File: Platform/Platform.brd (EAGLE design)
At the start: 97.8 x 36.8 mm, 30 parts, among them U1 LCD-16X2NOSILK, U2 LM2574N, X1 USBSMD, Y1 RESONATORSMD

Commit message: prototype 3
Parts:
- removed C10: 220uf, SparkFun:CPOL-RADIAL-100UF-25V
- removed C7: 4.7uf, SparkFun:CPOL-RADIAL-100UF-25V
- removed LOGO1: OSHW_LOGO_10MIL, ohw-logo:OSHW_10X200_NOTEXT_COPPER
- removed SG1: BUZZERPTH, SparkFun:BUZZER-12MM
- removed U1: LCD-16X2NOSILK, SparkFun:LCD-16X2_NOSILK
- added C4: 68uf, Dustin:F80
- added C5: 120uf, Dustin:10X8CAP
- added JP1: M14B, Dustin:1X14B
- added LCDCON: (no value), con-harting:CON14
- added LED2: RED, SparkFun:LED-1206
- added LINK1, LINK2, LINK3, LINK4: LINK, Dustin:ISOLATOR
- added R4: TRIMPOTSMD, SparkFun:TRIMPOT-3MM
- added SG2: BUZZERSMD, SparkFun:BUZZER-CMT1603
- C8: value 22uf -> 4.7uf; device SparkFun:CPOL-RADIAL-100UF-25V -> Dustin:CAP-B
- L2: value 330uH -> 100uH; device SparkFun:INDUCTOR-1206 -> SparkFun:0805
- LED1: value (none) -> GRN; device SparkFun:LED3MM -> SparkFun:LED-1206
- R3: value 10k -> 220; device SparkFun:TRIM_POT_PTH -> SparkFun:0805
- SCHOTTKEY: value 11DQ06 -> (none); device SparkFun:DIODE-ZENER -> Dustin:SOD-123
- U$1: value FT232RL -> FT232RLSSOP; device Dustin:TSSOP28 -> Dustin:SSOP28
- U$4: value DCJACK -> DCJACKSMD; device Dustin:DCPOWERSOCKETPJ-019 -> Dustin:JACK-SMD
- U2: device Dustin:8DILL -> Dustin:SOIC8
- moved S1 70.1 mm to (69.1, 41.3), turned to 0 degrees
- moved LED1 37.5 mm to (60.7, 41.7), turned to 0 degrees
- moved C2 33.8 mm to (33.4, 16.2)
- moved R1 32.8 mm to (31.2, 16.0)
- moved R3 31.0 mm to (61.2, 39.1)
- moved C8 24.4 mm to (60.5, 26.2), turned to 0 degrees
- moved SPI 20.6 mm to (14.0, 5.16), turned to 0 degrees
- moved U$4 12.9 mm to (25.4, -2.33), turned to 0 degrees
- moved C9 11.8 mm to (68.1, 26.7), turned to 0 degrees
- moved C1 11.4 mm to (64.7, 26.6)
- moved U$1 9.96 mm to (65.5, 18.0), turned to 0 degrees
- moved SCHOTTKEY 7.06 mm to (50.8, 2.54)
- moved U2 6.59 mm to (52.0, 7.11)
- moved L2 6.34 mm to (44.2, 12.6), turned to 0 degrees
- moved C6 6.28 mm to (73.4, 10.1), turned to 90 degrees
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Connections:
- removed net CTS: U$1.11
- new net FTDI-GND: C8.-, C9.1, LINK4.P$2, U$1.11, U$1.18, U$1.21, U$1.25, U$1.26, U$1.7
- new net FTDI-VCC: C6.-, C8.+, LINK3.P$1, U$1.20, U$1.4, U$3.2, X1.GND
- new net GNDLINK: C4.-, C5.-, LINK2.P$1, SCHOTTKEY.ANODE, U2.2, U2.3, U2.4
- new net N$7: LED1.C, R3.2
- new net VCCLINK: C5.+, L2.2, LINK1.P$1, U2.1
- net A1: now also JP1.3
- net A2: now also JP1.4
- net A3: now also JP1.5
- net A4: now also JP1.6
- net A5: now also JP1.7
- net A6: now also JP1.8
- net A7: now also JP1.9
- net CONTRAST: now also LCDCON.3, R4.2; no longer R3.2, U1.3
- net D10: now also LCDCON.4; no longer U1.4
- net D13/SCK: now also JP1.13, LED2.A; no longer LED1.A
- net D3: now also JP1.12
- net D4: now also LCDCON.14; no longer U1.14
- net D5: now also SG2.P$2; no longer SG1.-
- net D6: now also LCDCON.13; no longer U1.13
- net D7: now also LCDCON.12; no longer U1.12
- net D8: now also LCDCON.11; no longer U1.11
- net D9: now also LCDCON.6; no longer U1.6
- net GND: now also JP1.1, LCDCON.1, LCDCON.5, LINK2.P$2, LINK4.P$1, R3.1, R4.3, SG2.P$1; no longer C10.2, C6.-, C7.2, C8.2, C9.1, R3.3, SCHOTTKEY.P$2, SG1.+, U$1.18, U$1.21, U$1.25, U$1.26, U$1.7, U1.1, U1.16, U1.5, U2.2, U2.3, U2.4, X1.GND
- net N$2: now also LED2.C; no longer LED1.K
- net N$3: now also L2.1, SCHOTTKEY.CATHODE; no longer L2.P$1, SCHOTTKEY.P$1
- net RAW: now also C4.+; no longer C8.1
- net RAW_IN: now also U$4.1A, U$4.1B; no longer U$4.1C
- net RESET: now also JP1.14
- net RX: now also JP1.10
- net TX: now also JP1.11
- net VCC: now also JP1.2, LCDCON.2, LED1.A, LINK1.P$2, LINK3.P$2, R4.1; no longer C10.1, C7.1, L2.P$2, R3.1, U$1.20, U$1.4, U$3.2, U1.15, U1.2, U2.1
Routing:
- net FTDI-VCC: track 0.00 -> 65.2 mm
- net GNDLINK: track 0.00 -> 57.8 mm
- net RESET: track 86.6 -> 53.2 mm, vias 2 -> 0
- net D13/SCK: track 155.3 -> 122.1 mm, vias 1 -> 2
- net FTDI-GND: track 0.00 -> 33.2 mm
- net DTR: track 5.71 -> 32.8 mm
- net A0: track 108.1 -> 134.2 mm
- net VCC: track 236.7 -> 262.9 mm
- net VCCLINK: track 0.00 -> 25.6 mm
- net D11/MOSI: track 60.1 -> 35.5 mm
- net D12/MISO: track 99.6 -> 119.6 mm
- net RAW_IN: track 42.3 -> 62.0 mm, vias 0 -> 1
- net GND: track 331.7 -> 350.1 mm, vias 0 -> 2
- net N$4: track 34.4 -> 17.7 mm
- net N$5: track 33.8 -> 17.5 mm
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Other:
- board size 97.8 x 36.8 mm -> 91.7 x 42.9 mm

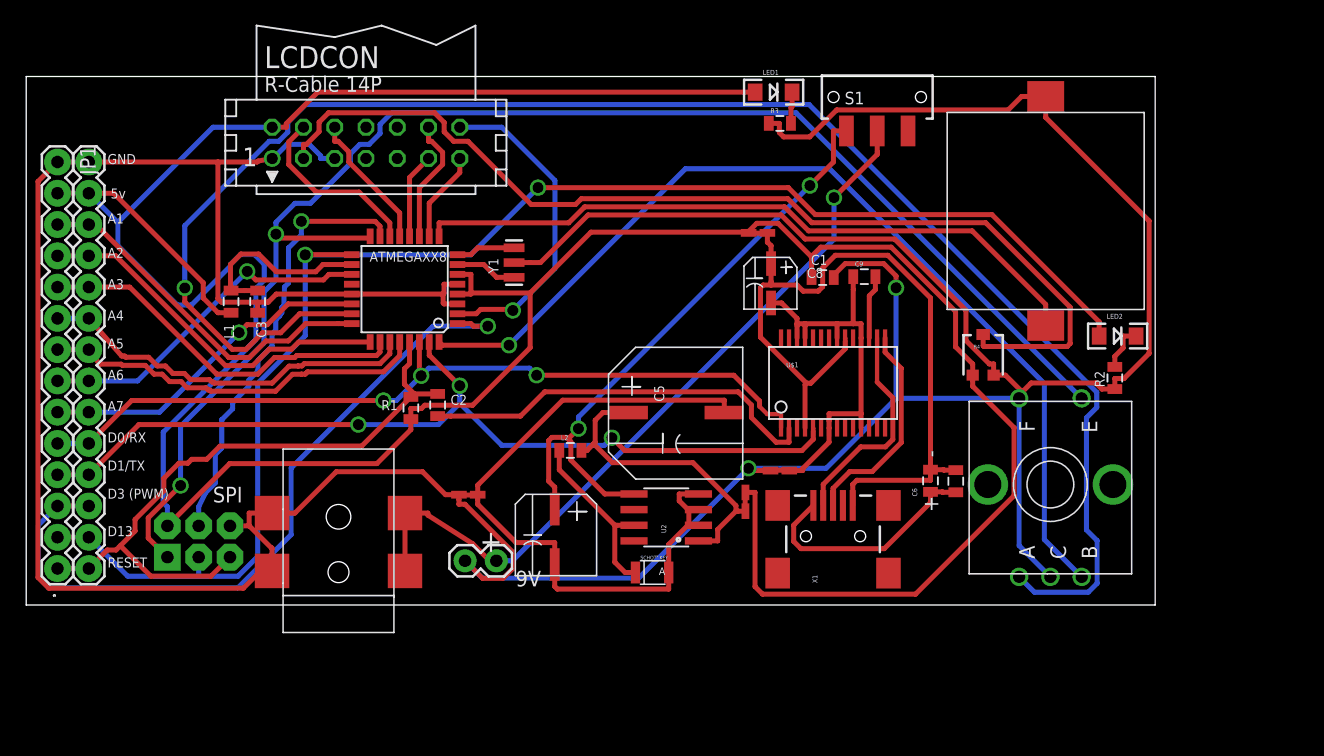
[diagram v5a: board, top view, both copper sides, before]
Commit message: Fixed some issues with the FTDI. Created Gerbers. Sent version off for manufacture.
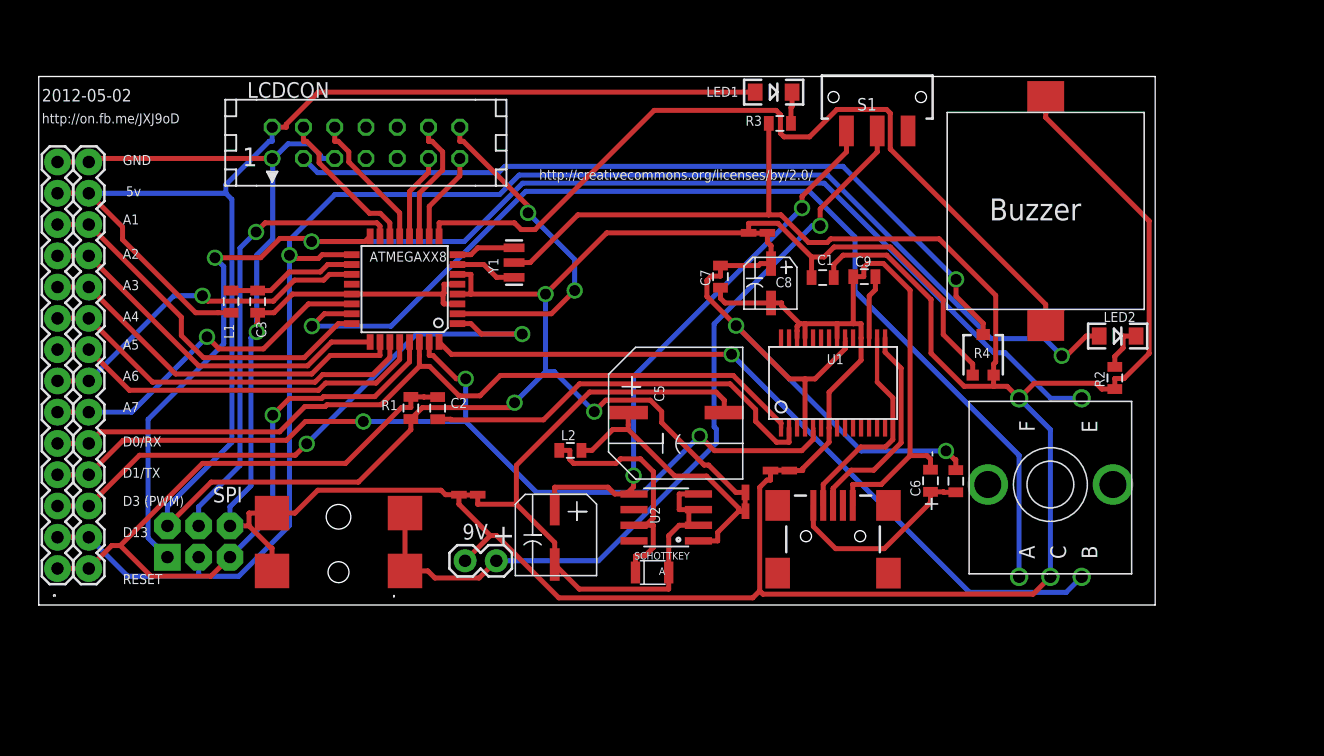
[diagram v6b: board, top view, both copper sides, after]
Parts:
- added C7: 0.1uf, SparkFun:0805
- moved C2 0.25 mm to (33.4, 16.0)
- renumbered LINK3 to FTDIVCCLINK, LINK4 to FTDIDGNDLINK, U$1 to U1
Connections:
- net N$1 renamed VBUS
- net N$4 renamed D-
- net N$5 renamed D+
- net N$6 renamed 3V3OUT
- net FTDI-GND: now also C6.-, C7.1, X1.GND; no longer U1.11
- net FTDI-VCC: now also C7.2; no longer C6.-, X1.GND
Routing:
- net GND: track 350.1 -> 302.5 mm, vias 2 -> 1
- net A0: track 134.2 -> 87.0 mm
- net VCC: track 262.9 -> 228.2 mm, vias 0 -> 3
- net FTDI-GND: track 33.2 -> 65.4 mm
- net RESET: track 53.2 -> 75.2 mm, vias 0 -> 1
- net CONTRAST: track 83.4 -> 62.9 mm, vias 0 -> 1
- net D2: track 79.4 -> 61.1 mm
- net FTDI-VCC: track 65.2 -> 53.3 mm, vias 0 -> 2
- net D5: track 55.9 -> 67.3 mm
- net D3: track 60.3 -> 49.1 mm, vias 1 -> 2
- net D12/MISO: track 119.6 -> 113.1 mm
- net N$3: track 14.5 -> 20.2 mm
- net RAW: track 50.6 -> 45.3 mm
- net AVCC: track 15.4 -> 10.7 mm
- net D13/SCK: track 122.1 -> 126.6 mm
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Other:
- board size 91.7 x 42.9 mm -> 90.7 x 42.9 mm
- board text added: "2012-05-02"
- board text added: "Buzzer"
- board text added: "http://creativecommons.org/licenses/by/2.0/"
- board text added: "http://on.fb.me/JXJ9oD"

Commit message: updates from prototype 3
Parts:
- removed U2: LM2574N, Dustin:SOIC8
- added LOGO1: OSHW_LOGO_10MILX0750-NT, ohw-logo:OSHW_10X750_NOTEXT
- added U$1: LM2594, Dustin:SOIC8
- C8: device Dustin:CAP-B -> SparkFun:0805
- LED1, LED2: device SparkFun:LED-1206 -> SparkFun:LED-0603
- S1: device SparkFun:SWITCH-SPDT-SMD -> Dustin:SWITCH-SPDT-SMT
- moved LED1 5.59 mm to (66.3, 41.7), turned to 270 degrees
- moved C7 5.08 mm to (61.5, 26.7)
- moved FTDIVCCLINK 5.08 mm to (64.5, 30.2)
- moved L2 5.08 mm to (49.3, 12.6)
- moved SCHOTTKEY 5.08 mm to (55.9, 2.54)
- moved C3 5.08 mm to (23.9, 24.6)
- moved LCDCON 5.08 mm to (32.7, 37.5)
- moved R1 5.08 mm to (36.3, 16.0)
- moved U$4 5.08 mm to (30.4, -2.33)
- moved JP2 5.08 mm to (10.2, 36.0)
- moved 9V 5.08 mm to (43.3, 3.59)
- moved ATMEGAXX8 5.08 mm to (35.8, 25.7)
- moved C1 5.08 mm to (69.8, 26.6)
- moved C2 5.08 mm to (38.5, 16.0)
- moved C4 5.08 mm to (48.0, 5.59)
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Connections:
- net FTDI-GND: now also C8.2; no longer C8.-
- net FTDI-VCC: now also C8.1; no longer C8.+
- net GND: now also U$4.1A, U$4.1B; no longer U$4.2, U$4.3
- net GNDLINK: now also U$1.5, U$1.6; no longer U2.2, U2.3, U2.4
- net N$3: now also U$1.8; no longer U2.7
- net RAW: now also U$1.7; no longer U2.5
- net RAW_IN: now also U$4.2, U$4.3; no longer U$4.1A, U$4.1B
- net VCCLINK: now also U$1.4; no longer U2.1
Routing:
- net VCC: track 228.2 -> 264.2 mm, vias 3 -> 1
- net RESET: track 75.2 -> 51.4 mm
- net D3: track 49.1 -> 62.6 mm, vias 2 -> 1
- net RAW_IN: track 66.1 -> 77.5 mm
- net FTDI-VCC: track 53.3 -> 63.6 mm, vias 2 -> 0
- net RX: track 67.0 -> 73.9 mm
- net GND: track 302.5 -> 296.2 mm, vias 1 -> 3
- net A7: track 28.4 -> 33.8 mm
- net RAW: track 45.3 -> 50.5 mm
- net A6: track 27.8 -> 32.9 mm
- net A4: track 31.2 -> 36.3 mm
- net A5: track 31.6 -> 36.7 mm
- net A3: track 30.8 -> 35.9 mm
- net A2: track 29.9 -> 35.0 mm
- net A1: track 30.4 -> 35.0 mm
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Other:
- board size 90.7 x 42.9 mm -> 95.8 x 42.9 mm
- board text added: "2012-05-12"
- board text added: "By Dustin Andrews and David Andrews"
- board text added: "Robotit Minion Starter Kit"
- board text removed: "2012-05-02"

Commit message: prototype 4
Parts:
- LED1, LED2: device SparkFun:LED-0603 -> SparkFun:LED-0805
- moved LOGO1 3.36 mm to (89.3, 12.0)
- moved U$2 1.58 mm to (89.5, 1.32)
- moved LED1 0.89 mm to (67.2, 41.7), turned to 0 degrees
- moved LED2 0.59 mm to (93.4, 21.3), turned to 0 degrees
- moved SG2 0.20 mm to (87.9, 31.8)
- renumbered U$1 to SWITCHREG
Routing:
- net GND: track 296.2 -> 321.8 mm, vias 3 -> 1
- net VCC: track 264.2 -> 253.0 mm, vias 1 -> 0
- net D5: track 65.6 -> 54.6 mm, vias 0 -> 2
- net D3: track 62.6 -> 71.6 mm
- net A0: track 84.1 -> 75.9 mm
- net D12/MISO: track 112.2 -> 115.9 mm
- net A7: track 33.8 -> 32.6 mm
- net CONTRAST: track 62.3 -> 63.5 mm
- net GNDLINK: track 58.6 -> 59.7 mm
- net D11/MOSI: track 37.4 -> 38.4 mm
- net RESET: track 51.4 -> 52.3 mm
- net FTDI-VCC: track 63.6 -> 62.7 mm
- net RAW: track 50.5 -> 51.2 mm
- net TX: track 78.8 -> 78.2 mm
- net D2: track 61.1 -> 61.7 mm
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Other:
- board size 95.8 x 42.9 mm -> 96.2 x 43.1 mm
- board text added: "D3-PWM"
